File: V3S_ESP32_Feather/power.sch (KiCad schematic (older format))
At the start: 32 parts, among them U1 V3S, U2 ADP322ACPZ-145-R7, U6 LT1963AxST-3.3

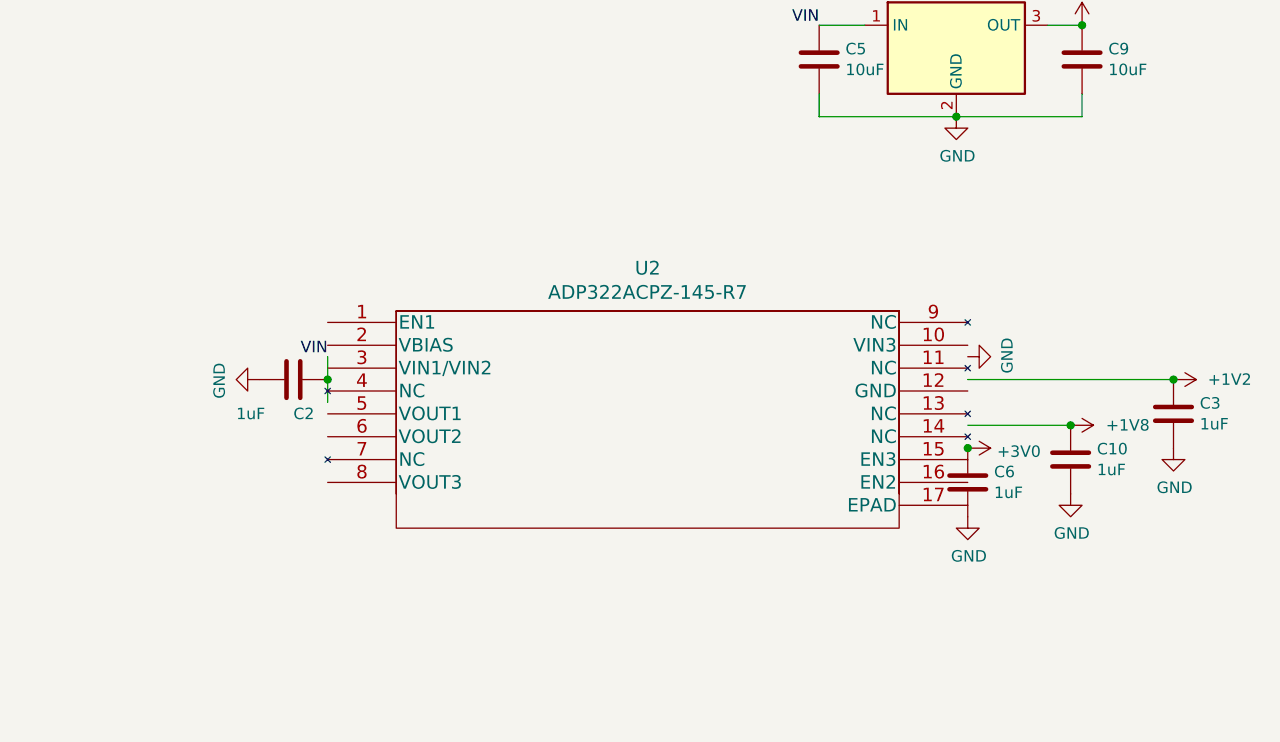
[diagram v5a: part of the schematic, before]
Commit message: fix adp322, optimize routing
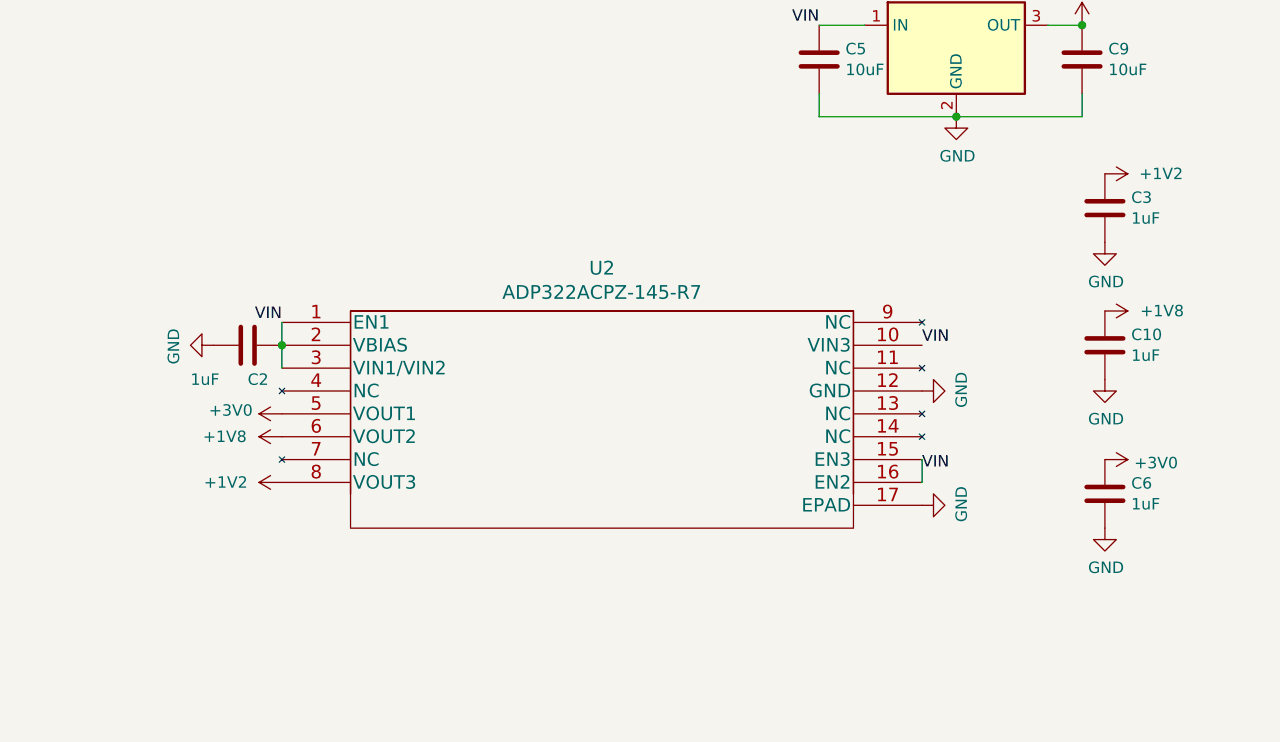
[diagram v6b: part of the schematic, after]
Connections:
- wire segments 81 -> 80
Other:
- moved on the sheet: C10, C2, C3, C6, U2
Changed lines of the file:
@@
 L power:+1V8 #PWR0131
 U 1 1 5BAA9AAB
-P 10400 5750
-F 0 "#PWR0131" H 10400 5600 50  0001 C CNN
-F 1 "+1V8" V 10400 6000 50  0000 C CNN
-F 2 "" H 10400 5750 50  0001 C CNN
-F 3 "" H 10400 5750 50  0001 C CNN
-	1    10400 5750
+P 10550 5250
+F 0 "#PWR0131" H 10550 5100 50  0001 C CNN
+F 1 "+1V8" V 10550 5500 50  0000 C CNN
+F 2 "" H 10550 5250 50  0001 C CNN
+F 3 "" H 10550 5250 50  0001 C CNN
+	1    10550 5250
 	0    1    1    0
 $EndComp
@@
 L power:+1V2 #PWR0148
 U 1 1 5CEEBC01
-P 10850 5550
-F 0 "#PWR0148" H 10850 5400 50  0001 C CNN
-F 1 "+1V2" V 10850 5700 50  0000 L CNN
-F 2 "" H 10850 5550 50  0001 C CNN
-F 3 "" H 10850 5550 50  0001 C CNN
-	1    10850 5550
+P 10550 4650
+F 0 "#PWR0148" H 10550 4500 50  0001 C CNN
+F 1 "+1V2" V 10550 4800 50  0000 L CNN
+F 2 "" H 10550 4650 50  0001 C CNN
+F 3 "" H 10550 4650 50  0001 C CNN
+	1    10550 4650
 	0    1    1    0
 $EndComp
@@
 Text Label 9300 4000 2    50   ~ 0
 VIN
-Text Label 7150 5450 2    50   ~ 0
+Text Label 6950 5300 2    50   ~ 0
 VIN
 $Comp
 L power:+3V0 #PWR0109
 U 1 1 5D8B36C1
-P 9950 5850
-F 0 "#PWR0109" H 9950 5700 50  0001 C CNN
-F 1 "+3V0" V 9965 5978 50  0000 L CNN
-F 2 "" H 9950 5850 50  0001 C CNN
-F 3 "" H 9950 5850 50  0001 C CNN
-	1    9950 5850
+P 10550 5900
+F 0 "#PWR0109" H 10550 5750 50  0001 C CNN
+F 1 "+3V0" V 10565 6028 50  0000 L CNN
+F 2 "" H 10550 5900 50  0001 C CNN
+F 3 "" H 10550 5900 50  0001 C CNN
+	1    10550 5900
 	0    1    1    0
 $EndComp
@@
 L Device:C C3
 U 1 1 5D8753D7
-P 10850 5700
-F 0 "C3" H 10965 5746 50  0000 L CNN
-F 1 "1uF" H 10965 5655 50  0000 L CNN
-F 2 "Capacitor_SMD:C_0201_0603Metric" H 10888 5550 50  0001 C CNN
-F 3 "~" H 10850 5700 50  0001 C CNN
-	1    10850 5700
+P 10550 4800
+F 0 "C3" H 10665 4846 50  0000 L CNN
+F 1 "1uF" H 10665 4755 50  0000 L CNN
+F 2 "Capacitor_SMD:C_0201_0603Metric" H 10588 4650 50  0001 C CNN
+F 3 "~" H 10550 4800 50  0001 C CNN
+	1    10550 4800
 	1    0    0    -1
 $EndComp
@@
 L Device:C C6
 U 1 1 5D87A551
-P 9950 6000
-F 0 "C6" H 10065 6046 50  0000 L CNN
-F 1 "1uF" H 10065 5955 50  0000 L CNN
-F 2 "Capacitor_SMD:C_0201_0603Metric" H 9988 5850 50  0001 C CNN
-F 3 "~" H 9950 6000 50  0001 C CNN
-	1    9950 6000
+P 10550 6050
+F 0 "C6" H 10665 6096 50  0000 L CNN
+F 1 "1uF" H 10665 6005 50  0000 L CNN
+F 2 "Capacitor_SMD:C_0201_0603Metric" H 10588 5900 50  0001 C CNN
+F 3 "~" H 10550 6050 50  0001 C CNN
+	1    10550 6050
 	1    0    0    -1
 $EndComp
@@
 L Device:C C10
 U 1 1 5D87C4CD
-P 10400 5900
-F 0 "C10" H 10515 5946 50  0000 L CNN
-F 1 "1uF" H 10515 5855 50  0000 L CNN
-F 2 "Capacitor_SMD:C_0201_0603Metric" H 10438 5750 50  0001 C CNN
-F 3 "~" H 10400 5900 50  0001 C CNN
-	1    10400 5900
+P 10550 5400
+F 0 "C10" H 10665 5446 50  0000 L CNN
+F 1 "1uF" H 10665 5355 50  0000 L CNN
+F 2 "Capacitor_SMD:C_0201_0603Metric" H 10588 5250 50  0001 C CNN
+F 3 "~" H 10550 5400 50  0001 C CNN
+	1    10550 5400
 	1    0    0    -1
 $EndComp
@@
 L power:GND #PWR0137
 U 1 1 5D88350A
-P 10850 5850
-F 0 "#PWR0137" H 10850 5600 50  0001 C CNN
-F 1 "GND" H 10855 5677 50  0000 C CNN
-F 2 "" H 10850 5850 50  0001 C CNN
-F 3 "" H 10850 5850 50  0001 C CNN
-	1    10850 5850
+P 10550 4950
+F 0 "#PWR0137" H 10550 4700 50  0001 C CNN
+F 1 "GND" H 10555 4777 50  0000 C CNN
+F 2 "" H 10550 4950 50  0001 C CNN
+F 3 "" H 10550 4950 50  0001 C CNN
+	1    10550 4950
 	1    0    0    -1
 $EndComp
@@
 L power:GND #PWR0140
 U 1 1 5D8857BD
-P 9950 6150
-F 0 "#PWR0140" H 9950 5900 50  0001 C CNN
-F 1 "GND" H 9955 5977 50  0000 C CNN
-F 2 "" H 9950 6150 50  0001 C CNN
-F 3 "" H 9950 6150 50  0001 C CNN
-	1    9950 6150
+P 10550 6200
+F 0 "#PWR0140" H 10550 5950 50  0001 C CNN
+F 1 "GND" H 10555 6027 50  0000 C CNN
+F 2 "" H 10550 6200 50  0001 C CNN
+F 3 "" H 10550 6200 50  0001 C CNN
+	1    10550 6200
 	1    0    0    -1
 $EndComp
@@
 L power:GND #PWR0141
 U 1 1 5D886F9B
-P 10400 6050
-F 0 "#PWR0141" H 10400 5800 50  0001 C CNN
-F 1 "GND" H 10405 5877 50  0000 C CNN
-F 2 "" H 10400 6050 50  0001 C CNN
-F 3 "" H 10400 6050 50  0001 C CNN
-	1    10400 6050
+P 10550 5550
+F 0 "#PWR0141" H 10550 5300 50  0001 C CNN
+F 1 "GND" H 10555 5377 50  0000 C CNN
+F 2 "" H 10550 5550 50  0001 C CNN
+F 3 "" H 10550 5550 50  0001 C CNN
+	1    10550 5550
 	1    0    0    -1
 $EndComp
@@
 L 2019-06-13_12-28-51:ADP322ACPZ-145-R7 U2
 U 1 1 5D909DE6
-P 7150 5450
-F 0 "U2" H 8550 5837 60  0000 C CNN
-F 1 "ADP322ACPZ-145-R7" H 8550 5731 60  0000 C CNN
-F 2 "QFN50P300X300X90-17N:QFN50P300X300X90-17N" H 8550 5690 60  0001 C CNN
-F 3 "" H 7150 5450 60  0000 C CNN
-	1    7150 5450
-	1    0    0    -1
-$EndComp
-Wire Wire Line
-	7150 5450 7150 5550
-Wire Wire Line
-	7150 5650 7150 5550
-Connection ~ 7150 5550
+P 6950 5450
+F 0 "U2" H 8350 5837 60  0000 C CNN
+F 1 "ADP322ACPZ-145-R7" H 8350 5731 60  0000 C CNN
+F 2 "QFN50P300X300X90-17N:QFN50P300X300X90-17N" H 8350 5690 60  0001 C CNN
+F 3 "" H 6950 5450 60  0000 C CNN
+	1    6950 5450
+	1    0    0    -1
+$EndComp
 $Comp
 L Device:C C2
 U 1 1 5D91C041
-P 7000 5550
-F 0 "C2" V 7150 5550 50  0000 L CNN
-F 1 "1uF" V 7150 5300 50  0000 L CNN
-F 2 "Capacitor_SMD:C_0201_0603Metric" H 7038 5400 50  0001 C CNN
-F 3 "~" H 7000 5550 50  0001 C CNN
-	1    7000 5550
+P 6800 5400
+F 0 "C2" V 6950 5400 50  0000 L CNN
+F 1 "1uF" V 6950 5150 50  0000 L CNN
+F 2 "Capacitor_SMD:C_0201_0603Metric" H 6838 5250 50  0001 C CNN
+F 3 "~" H 6800 5400 50  0001 C CNN
+	1    6800 5400
 	0    1    1    0
 $EndComp
@@
 L power:GND #PWR0103
 U 1 1 5D91C047
-P 6850 5550
-F 0 "#PWR0103" H 6850 5300 50  0001 C CNN
-F 1 "GND" H 6855 5377 50  0000 C CNN
-F 2 "" H 6850 5550 50  0001 C CNN
-F 3 "" H 6850 5550 50  0001 C CNN
-	1    6850 5550
+P 6650 5400
+F 0 "#PWR0103" H 6650 5150 50  0001 C CNN
+F 1 "GND" H 6655 5227 50  0000 C CNN
+F 2 "" H 6650 5400 50  0001 C CNN
+F 3 "" H 6650 5400 50  0001 C CNN
+	1    6650 5400
 	0    1    1    0
 $EndComp
@@
 Wire Wire Line
 	7600 3100 7600 3250
-Connection ~ 9950 5850
-Wire Wire Line
-	9950 5750 10400 5750
-Connection ~ 10400 5750
-Wire Wire Line
-	10850 5550 9950 5550
-Connection ~ 10850 5550
 $Comp
 L power:GND #PWR0104
 U 1 1 5D95784E
-P 9950 5450
-F 0 "#PWR0104" H 9950 5200 50  0001 C CNN
-F 1 "GND" H 9955 5277 50  0000 C CNN
-F 2 "" H 9950 5450 50  0001 C CNN
-F 3 "" H 9950 5450 50  0001 C CNN
-	1    9950 5450
+P 9750 6100
+F 0 "#PWR0104" H 9750 5850 50  0001 C CNN
+F 1 "GND" H 9755 5927 50  0000 C CNN
+F 2 "" H 9750 6100 50  0001 C CNN
+F 3 "" H 9750 6100 50  0001 C CNN
+	1    9750 6100
 	0    -1   -1   0
 $EndComp
@@
 Wire Wire Line
 	3450 1200 3650 1200
+Wire Wire Line
+	6950 5500 6950 5400
+Connection ~ 6950 5400
+Wire Wire Line
+	6950 5400 6950 5300
+Text Label 9750 5400 0    50   ~ 0
+VIN
+Text Label 9750 5950 0    50   ~ 0
+VIN
+Wire Wire Line
+	9750 5900 9750 6000
+$Comp
+L power:GND #PWR?
+U 1 1 5DC48C02
+P 9750 5600
+F 0 "#PWR?" H 9750 5350 50  0001 C CNN
+F 1 "GND" H 9755 5427 50  0000 C CNN
+F 2 "" H 9750 5600 50  0001 C CNN
+F 3 "" H 9750 5600 50  0001 C CNN
+	1    9750 5600
+	0    -1   -1   0
+$EndComp
+$Comp
+L power:+1V2 #PWR?
+U 1 1 5DC555EC
+P 6950 6000
+F 0 "#PWR?" H 6950 5850 50  0001 C CNN
+F 1 "+1V2" V 6950 6150 50  0000 L CNN
+F 2 "" H 6950 6000 50  0001 C CNN
+F 3 "" H 6950 6000 50  0001 C CNN
+	1    6950 6000
+	0    -1   -1   0
+$EndComp
+$Comp
+L power:+1V8 #PWR?
+U 1 1 5DC57383
+P 6950 5800
+F 0 "#PWR?" H 6950 5650 50  0001 C CNN
+F 1 "+1V8" V 6950 6050 50  0000 C CNN
+F 2 "" H 6950 5800 50  0001 C CNN
+F 3 "" H 6950 5800 50  0001 C CNN
+	1    6950 5800
+	0    -1   -1   0
+$EndComp
+$Comp
+L power:+3V0 #PWR?
+U 1 1 5DC590A3
+P 6950 5700
+F 0 "#PWR?" H 6950 5550 50  0001 C CNN
+F 1 "+3V0" V 6965 5828 50  0000 L CNN
+F 2 "" H 6950 5700 50  0001 C CNN
+F 3 "" H 6950 5700 50  0001 C CNN
+	1    6950 5700
+	0    -1   -1   0
+$EndComp
 $EndSCHEMATC

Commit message: Move via from pad and rebuild fab files
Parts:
- C48, C49, C54, C61, C63, C64, C65: value 100nF -> 0.1uF
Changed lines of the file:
@@
 P 4900 1050
 F 0 "C48" H 5015 1096 50  0000 L CNN
-F 1 "100nF" H 5000 850 50  0000 L CNN
+F 1 "0.1uF" H 5000 850 50  0000 L CNN
 F 2 "Capacitor_SMD:C_0201_0603Metric" H 4938 900 50  0001 C CNN
 F 3 "~" H 4900 1050 50  0001 C CNN
@@
 P 7450 1050
 F 0 "C49" H 7565 1096 50  0000 L CNN
-F 1 "100nF" H 7550 850 50  0000 L CNN
+F 1 "0.1uF" H 7550 850 50  0000 L CNN
 F 2 "Capacitor_SMD:C_0201_0603Metric" H 7488 900 50  0001 C CNN
 F 3 "~" H 7450 1050 50  0001 C CNN
@@
 P 2300 1050
 F 0 "C54" H 2100 1150 50  0000 L CNN
-F 1 "100nF" H 2050 950 50  0000 L CNN
+F 1 "0.1uF" H 2050 950 50  0000 L CNN
 F 2 "Capacitor_SMD:C_0201_0603Metric" H 2338 900 50  0001 C CNN
 F 3 "~" H 2300 1050 50  0001 C CNN
@@
 P 6150 1050
 F 0 "C63" H 6265 1096 50  0000 L CNN
-F 1 "100nF" H 6250 850 50  0000 L CNN
+F 1 "0.1uF" H 6250 850 50  0000 L CNN
 F 2 "Capacitor_SMD:C_0201_0603Metric" H 6188 900 50  0001 C CNN
 F 3 "~" H 6150 1050 50  0001 C CNN
@@
 P 950 900
 F 0 "C64" V 698 900 50  0000 C CNN
-F 1 "100nF" V 789 900 50  0000 C CNN
+F 1 "0.1uF" V 789 900 50  0000 C CNN
 F 2 "Capacitor_SMD:C_0201_0603Metric" H 988 750 50  0001 C CNN
 F 3 "~" H 950 900 50  0001 C CNN
@@
 P 1450 900
 F 0 "C65" V 1198 900 50  0000 C CNN
-F 1 "100nF" V 1289 900 50  0000 C CNN
+F 1 "0.1uF" V 1289 900 50  0000 C CNN
 F 2 "Capacitor_SMD:C_0201_0603Metric" H 1488 750 50  0001 C CNN
 F 3 "~" H 1450 900 50  0001 C CNN
@@
 P 3650 1050
 F 0 "C61" H 3500 950 50  0000 C CNN
-F 1 "100nF" H 3500 1150 50  0000 C CNN
+F 1 "0.1uF" H 3500 1150 50  0000 C CNN
 F 2 "Capacitor_SMD:C_0201_0603Metric" H 3688 900 50  0001 C CNN
 F 3 "~" H 3650 1050 50  0001 C CNN
